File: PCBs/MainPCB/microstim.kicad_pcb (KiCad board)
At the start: 2 copper layers, 124.5 x 79.5 mm, 87 parts, among them J1 Conn_Coaxial, J10 Conn_Coaxial, J11 Screw_Terminal_01x02, J12 Conn_Coaxial, J3 Screw_Terminal_01x02, J5 Conn_Coaxial, J7 Screw_Terminal_01x02, J9 Screw_Terminal_01x02, U1 Teensy3.5, U10 AD7321, U11 INA826, U12 AD8276, U13 AD8276, U14 INA826, U15 OPA197, U16 DG509ACWE, U17 OPA197, U18 DG509ACWE, U19 DG419LDY, U2 CC3-0512DF-E, U20 DG419LDY, U3 L78L05_SO8, U4 L78L12_SO8, U5 ISO7760, U6 AD1582, U7 ISO7341C, U8 L79L12_SO8, U9 MCP4922

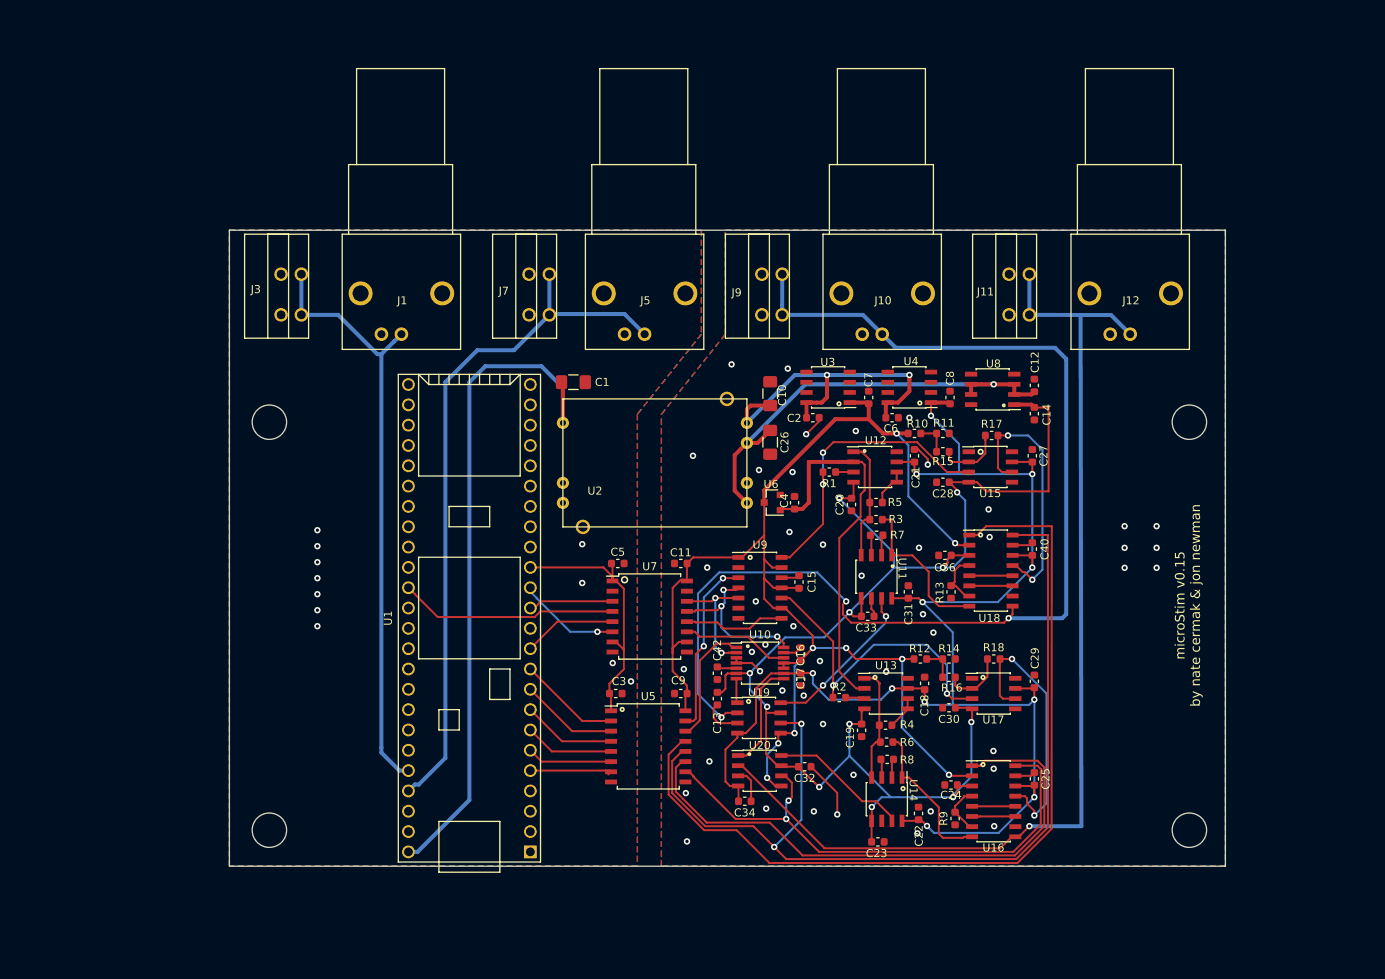
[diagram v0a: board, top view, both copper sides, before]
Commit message: almost done with revision 3. 12v regs removed, GPIO breakout and indicator LEDs added, layout cleaned up
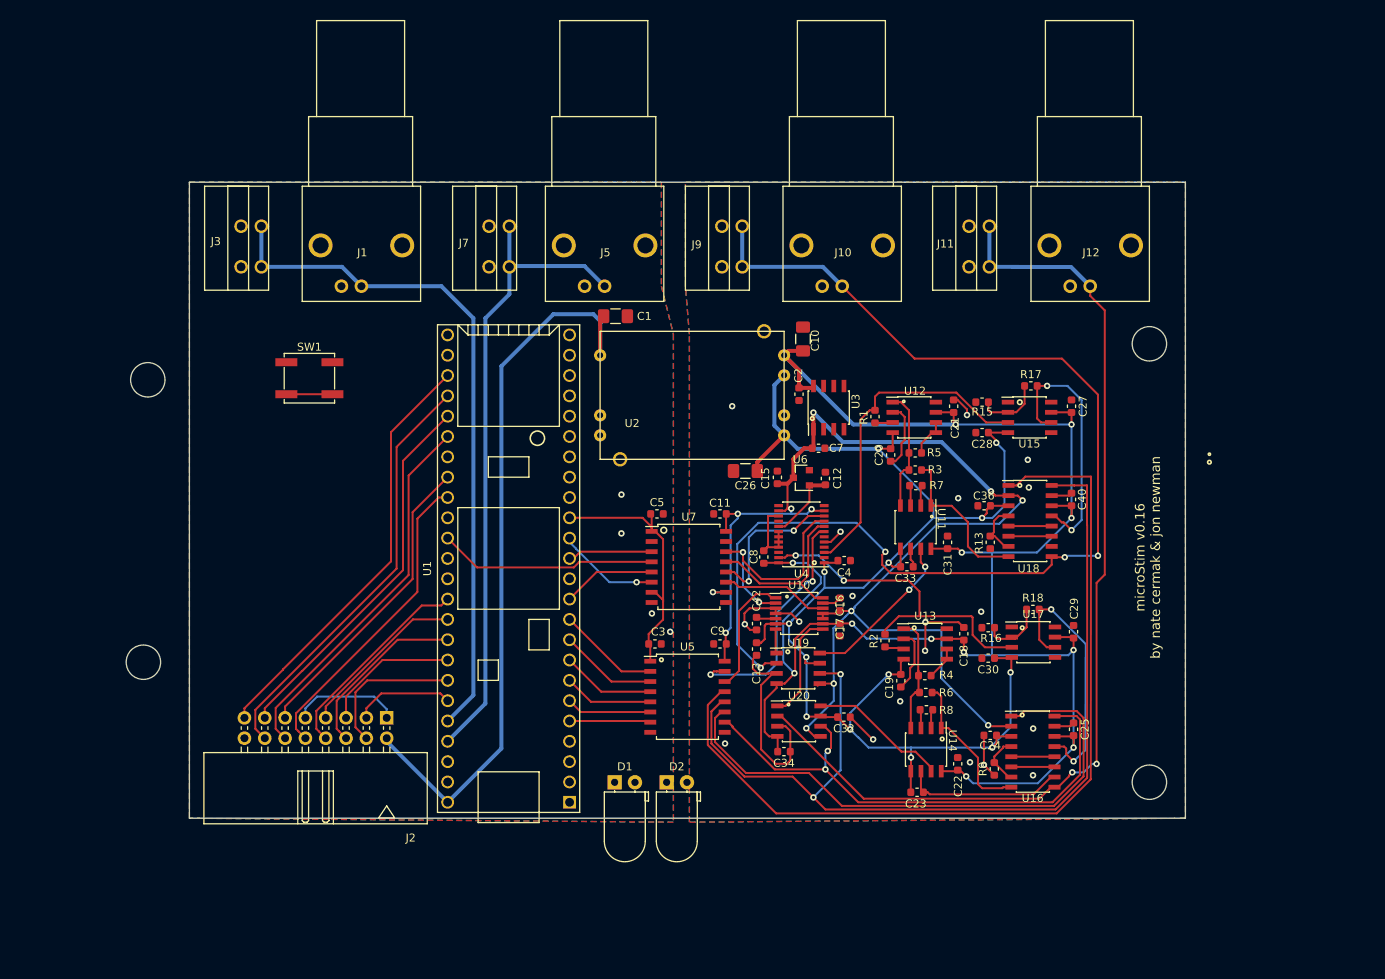
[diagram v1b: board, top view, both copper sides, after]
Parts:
- removed C14, C6: 1uF, Capacitor_SMD:C_0603_1608Metric
- removed R10, R12: 100, Resistor_SMD:R_0603_1608Metric
- removed R11, R14: 180, Resistor_SMD:R_0603_1608Metric
- removed U8: L79L12_SO8, Package_SO:SOIC-8_3.9x4.9mm_P1.27mm
- removed U9: MCP4922, Package_SO:SOIC-14_3.9x8.7mm_P1.27mm
- added D1: LED, LED_THT:LED_D5.0mm_Horizontal_O1.27mm_Z3.0mm, F.Cu at (135.7, 127.0)
- added D2: LED, LED_THT:LED_D5.0mm_Horizontal_O1.27mm_Z3.0mm, F.Cu at (142.2, 127.0)
- added J2: Conn_02x08_Counter_Clockwise, Connector_Multicomp:Multicomp_MC9A22-1634_2x08_P2.54mm_Horizontal, F.Cu at (107.2, 119.0)
- added SW1: SW_Push, Button_Switch_SMD:SW_SPST_EVPBF, F.Cu at (97.5, 76.5)
- C4, C8: value 1uF -> 0.1uF
- R17, R18: value 4k -> 500
- R3, R6: value 250 -> 100
- R7, R8: value 1.2k -> 1.8k
- U4: value L78L12_SO8 -> AD5752; footprint Package_SO:SOIC-8_3.9x4.9mm_P1.27mm -> Package_SO:TSSOP-24_4.4x7.8mm_P0.65mm
- moved C8 30.6 mm to (154.3, 98.8)
- moved C12 28.6 mm to (162.0, 89.0)
- moved H1 26.2 mm to (76.8, 112.0)
- moved U4 22.8 mm to (159.0, 96.0)
- moved H3 16.1 mm to (77.3, 76.7)
- moved C15 13.4 mm to (156.0, 88.9)
- moved H2 11.0 mm to (202.5, 72.2)
- moved C1 9.79 mm to (135.8, 68.8)
- moved U2 9.64 mm to (133.8, 86.6)
- moved C4 9.53 mm to (164.3, 99.3), turned to 180 degrees
- moved R2 9.14 mm to (169.4, 109.3), turned to 90 degrees
- moved R1 8.98 mm to (168.2, 81.3), turned to 90 degrees
- moved C7 8.92 mm to (161.1, 85.3), turned to 180 degrees
- moved U17 8.11 mm to (188.0, 109.5)
- moved C10 7.97 mm to (159.2, 71.6)
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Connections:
- C12 pad 2: -15V -> 2.5V
- C13 pad 1: -12V -> -15V
- C16 pad 1: +12V -> +15V
- C18 pad 2: +12V -> +15V
- C19 pad 1: -12V -> -15V
- C20 pad 1: -12V -> -15V
- C21 pad 2: +12V -> +15V
- C22 pad 2: +12V -> +15V
- C23 pad 2: -12V -> -15V
- C24 pad 2: -12V -> -15V
- C25 pad 2: +12V -> +15V
- C27 pad 2: +12V -> +15V
- C28 pad 1: -12V -> -15V
- C29 pad 2: +12V -> +15V
- C30 pad 1: -12V -> -15V
- C31 pad 2: +12V -> +15V
- C32 pad 2: -12V -> -15V
- C33 pad 2: -12V -> -15V
- C34 pad 2: +12V -> +15V
- C36 pad 2: -12V -> -15V
- C4 pad 2: 2.5V -> -15V
- C40 pad 2: +12V -> +15V
- C8 pad 2: +12V -> +15V
- R15 pad 1: Net-(R10-Pad1) -> GNDREF
- R16 pad 1: Net-(R12-Pad1) -> GNDREF
- U1 pad 39: Net-(U1-Pad39) -> GND
- U1 pad 43: Net-(U1-Pad43) -> GPIO5
- U1 pad 44: Net-(U1-Pad44) -> GPIO4
- U1 pad 45: Net-(U1-Pad45) -> GPIO3
- U1 pad 46: Net-(U1-Pad46) -> GPIO2
- U1 pad 47: Net-(U1-Pad47) -> GPIO1
- U1 pad 48: Net-(U1-Pad48) -> GPIO0
- U1 pad 51: +3V3 -> Net-(U1-Pad51)
- U10 pad 6: -12V -> -15V
- U10 pad 9: +12V -> +15V
- U11 pad 5: -12V -> -15V
- U11 pad 8: +12V -> +15V
- U12 pad 2: 2.5V -> GNDREF
- U12 pad 4: -12V -> -15V
- U12 pad 7: +12V -> +15V
- U13 pad 2: 2.5V -> GNDREF
- U13 pad 4: -12V -> -15V
- U13 pad 7: +12V -> +15V
- U14 pad 5: -12V -> -15V
- U14 pad 8: +12V -> +15V
- U15 pad 4: -12V -> -15V
- U15 pad 7: +12V -> +15V
- U16 pad 14: +12V -> +15V
- U16 pad 3: -12V -> -15V
- U17 pad 4: -12V -> -15V
- U17 pad 7: +12V -> +15V
- U18 pad 14: +12V -> +15V
- U18 pad 3: -12V -> -15V
- U19 pad 4: +12V -> +15V
- U19 pad 7: -12V -> -15V
- U20 pad 4: +12V -> +15V
- U20 pad 7: -12V -> -15V
- U4 pad 1: +12V -> -15V
- U4 pad 2: GNDREF -> (no net)
- U4 pad 3: GNDREF -> DAC0
- U4 pad 4: Net-(U4-Pad4) -> (no net)
- U4 pad 5: Net-(U4-Pad5) -> GNDREF
- U4 pad 6: GNDREF -> (no net)
- U4 pad 7: GNDREF -> CS0i
- U4 pad 8: +15V -> SCK0i
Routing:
- net +12V: track 182.1 -> 0.00 mm, vias 11 -> 0
- net +15V: track 42.4 -> 223.0 mm, vias 2 -> 12
- net -12V: track 174.8 -> 0.00 mm, vias 11 -> 0
- net -15V: track 56.8 -> 183.3 mm, vias 1 -> 13
- net GNDREF: track 38.7 -> 117.1 mm, vias 46 -> 19
- net Net-(J2-Pad15): track 0.00 -> 53.3 mm
- net Net-(J2-Pad14): track 0.00 -> 53.2 mm
- net Net-(J2-Pad13): track 0.00 -> 47.2 mm
- net Net-(J2-Pad12): track 0.00 -> 47.1 mm
- net Net-(J2-Pad10): track 0.00 -> 39.1 mm
- net Net-(J2-Pad11): track 0.00 -> 38.5 mm
- net 2.5V: track 47.4 -> 9.22 mm
- net GPIO5: track 0.00 -> 26.1 mm
- net GPIO3: track 0.00 -> 22.2 mm
- net GPIO4: track 0.00 -> 21.2 mm
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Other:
- board text added: "microStim v0.16 by nate cermak & jon newman"
- board text removed: "microStim v0.15 by nate cermak & jon newman"

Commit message: major updates to isolate each output channel.
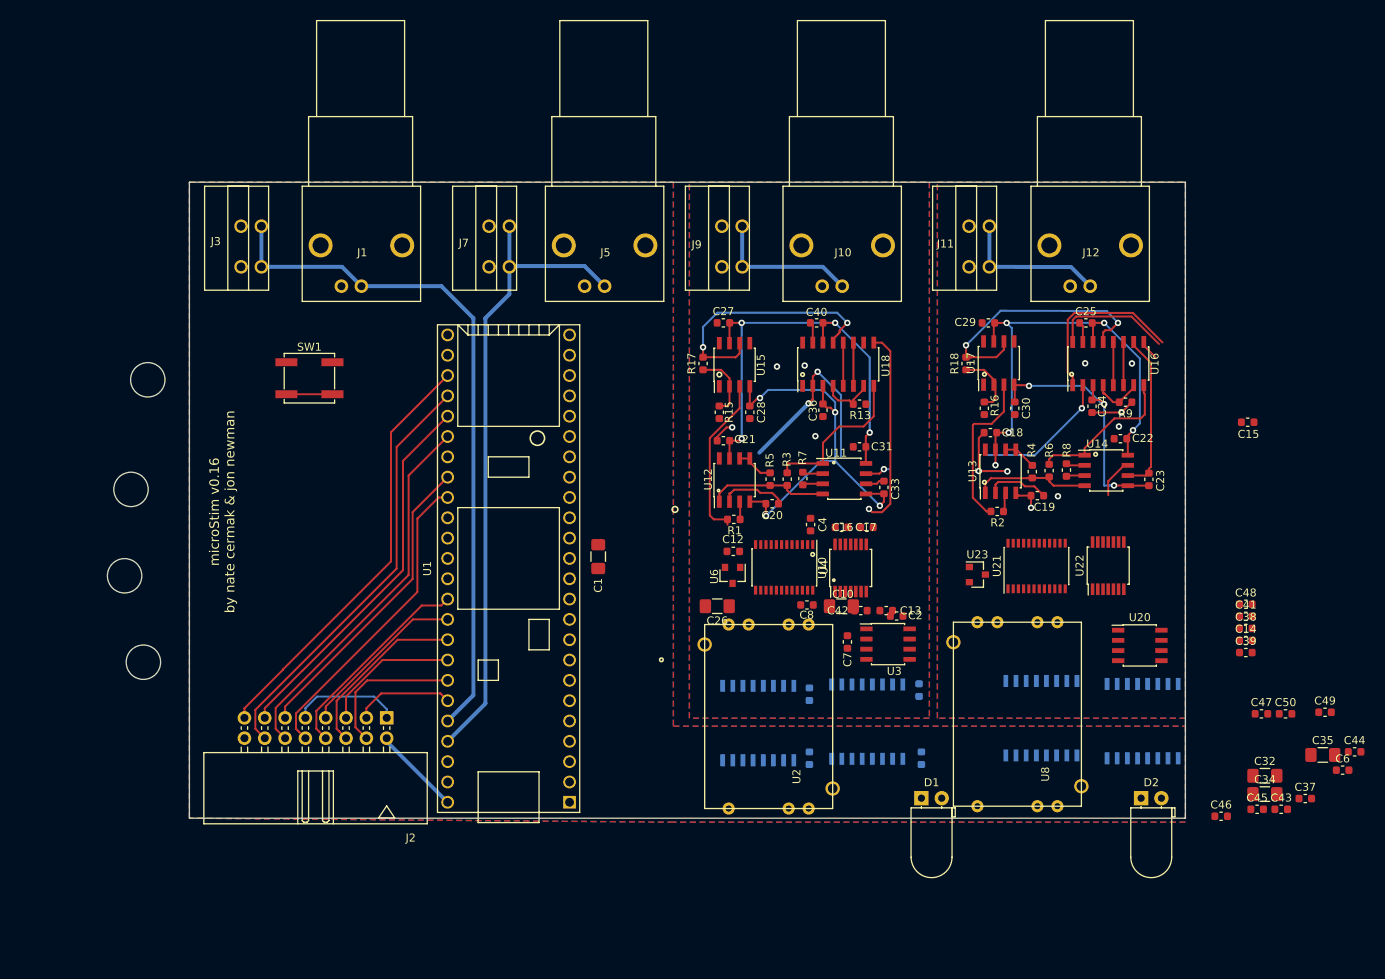
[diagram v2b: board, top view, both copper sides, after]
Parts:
- added C14: 0.1uF, Capacitor_SMD:C_0603_1608Metric, F.Cu at (214.6, 109.3)
- added C35: 10uF, Capacitor_SMD:C_1206_3216Metric_Pad1.42x1.75mm_HandSolder, F.Cu at (224.2, 123.6)
- added C37: 0.1uF, Capacitor_SMD:C_0603_1608Metric, F.Cu at (222.0, 129.0)
- added C38: 0.1uF, Capacitor_SMD:C_0603_1608Metric, F.Cu at (214.6, 107.8)
- added C39: 1uF, Capacitor_SMD:C_0603_1608Metric, F.Cu at (214.6, 110.8)
- added C41: 0.1uF, Capacitor_SMD:C_0603_1608Metric, F.Cu at (214.6, 106.3)
- added C43: 680nF, Capacitor_SMD:C_0603_1608Metric, F.Cu at (219.0, 130.4)
- added C44: 0.1uF, Capacitor_SMD:C_0603_1608Metric, F.Cu at (228.2, 123.2)
- added C45: 1uF, Capacitor_SMD:C_0603_1608Metric, F.Cu at (216.0, 130.4)
- added C46: 0.1uF, Capacitor_SMD:C_0603_1608Metric, F.Cu at (211.5, 131.3)
- added C47: 0.1uF, Capacitor_SMD:C_0603_1608Metric, F.Cu at (216.5, 118.5)
- added C48: 1uF, Capacitor_SMD:C_0603_1608Metric, F.Cu at (214.6, 104.8)
- added C49: 0.1uF, Capacitor_SMD:C_0603_1608Metric, F.Cu at (224.5, 118.3)
- added C50: 0.1uF, Capacitor_SMD:C_0603_1608Metric, F.Cu at (219.5, 118.5)
- added C6: 0.1uF, Capacitor_SMD:C_0603_1608Metric, F.Cu at (226.7, 125.5)
- added U21: AD5752, Package_SO:TSSOP-24_4.4x7.8mm_P0.65mm, F.Cu at (188.4, 100.0)
- added U22: AD7321, Package_SO:TSSOP-14_4.4x5mm_P0.65mm, F.Cu at (197.4, 99.9)
- added U23: AD1582, Package_TO_SOT_SMD:SOT-23, F.Cu at (181.0, 101.0)
- added U8: CC3-0512DF-E, microstim:CC3-0512DF-E, F.Cu at (194.0, 130.0)
- added U9: ISO7760, Package_SO:SOIC-16W_7.5x10.3mm_P1.27mm, B.Cu at (189.0, 119.0)
- C11, C3, C5, C9, U5, U7: moved to B.Cu
- C32, C34: value 0.1uF -> 10uF; footprint Capacitor_SMD:C_0603_1608Metric -> Capacitor_SMD:C_1206_3216Metric_Pad1.42x1.75mm_HandSolder
- U19: value DG419LDY -> ISO7341C; footprint Package_SO:SOIC-8_3.9x4.9mm_P1.27mm -> Package_SO:SOIC-16W_7.5x10.3mm_P1.27mm; moved to B.Cu
- U20: value DG419LDY -> L78L05_SO8
- moved H4 130.7 mm to (74.4, 101.2)
- moved H2 128.6 mm to (75.2, 90.4)
- moved C34 60.3 mm to (216.9, 128.5), turned to 0 degrees
- moved D2 59.3 mm to (201.5, 129.0)
- moved C15 59.2 mm to (214.8, 82.0), turned to 0 degrees
- moved C32 53.1 mm to (216.9, 126.2), turned to 0 degrees
- moved U2 52.4 mm to (162.9, 130.3), turned to 90 degrees
- moved C25 50.8 mm to (194.6, 69.6), turned to 0 degrees
- moved U16 49.4 mm to (197.4, 74.7), turned to 90 degrees
- moved R9 48.7 mm to (199.5, 79.5), turned to 180 degrees
- moved C23 48.7 mm to (202.4, 89.1), turned to 270 degrees
- moved C22 45.4 mm to (198.9, 84.1), turned to 0 degrees
- moved C5 45.0 mm to (174.0, 124.0), turned to 90 degrees
- moved C27 44.7 mm to (149.2, 69.6), turned to 0 degrees
- moved U20 43.6 mm to (201.3, 109.9)
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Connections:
- net 2.5V renamed 2.5V_0
- net CS0i renamed CS0_0i
- net CS1i renamed CS1_0i
- net DAC0 renamed DAC_0
- net IOUT0 renamed IOUT_0
- net IOUT1 renamed IOUT_1
- net MISO renamed MISO_0
- net MISOi renamed MISO_0i
- net MOSI renamed MOSI_0
- net MOSIi renamed MOSI_0i
- net NLDACi renamed NLDAC_0i
- net OE0i renamed OE0_0i
- net SCK0 renamed SCK_0
- net SCK0i renamed SCK_0i
- net VOUT0 renamed VOUT_0
- net VOUT1 renamed VOUT_1
- C10 pad 1: GNDREF -> GND_0
- C10 pad 2: +15V -> +15V_0
- C11 pad 1: +5V -> +5V_0
- C11 pad 2: GNDREF -> GND_0
- C12 pad 1: GNDREF -> GND_0
- C13 pad 1: -15V -> -15V_0
- C13 pad 2: GNDREF -> GND_0
- C15 pad 1: GNDREF -> GND_0
- C15 pad 2: +5V -> +5V_0
- C16 pad 1: +15V -> +15V_0
- C16 pad 2: GNDREF -> GND_0
- C17 pad 1: +5V -> +5V_0
- C17 pad 2: GNDREF -> GND_0
- C2 pad 1: GNDREF -> GND_0
- C2 pad 2: +15V -> +15V_0
- C20 pad 2: GNDREF -> GND_0
- C21 pad 1: GNDREF -> GND_0
- C26 pad 1: -15V -> -15V_0
- C26 pad 2: GNDREF -> GND_0
- C32 pad 1: GNDREF -> GND
- C32 pad 2: -15V -> VUSB
- C34 pad 1: GNDREF -> GND_1
- C34 pad 2: +15V -> +15V_1
- C4 pad 1: GNDREF -> GND_0
- C4 pad 2: -15V -> -15V_0
- C42 pad 2: GNDREF -> GND_0
- C7 pad 1: GNDREF -> GND_0
- C7 pad 2: +5V -> +5V_0
- C8 pad 1: GNDREF -> GND_0
- C8 pad 2: +15V -> +15V_0
- C9 pad 1: GNDREF -> GND_0
- C9 pad 2: +5V -> +5V_0
- J10 pad 1: OUT0 -> OUT_0
- J11 pad 1: OUT1 -> OUT_1
- J12 pad 1: OUT1 -> OUT_1
- J9 pad 1: OUT0 -> OUT_0
- R15 pad 1: GNDREF -> GND_0
- R2 pad 2: DAC1 -> DAC_1
- U1 pad 10: CS0 -> OE0_0
- U1 pad 11: NLDAC -> CS1_0
- U1 pad 12: Net-(U1-Pad12) -> CS0_0
- U1 pad 16: Net-(U1-Pad16) -> NLDAC_0
- U1 pad 2: Net-(U1-Pad2) -> MOSI_1
- U1 pad 24: Net-(U1-Pad24) -> SCK_1
- U1 pad 3: Net-(U1-Pad3) -> MISO_1
- U1 pad 4: Net-(U1-Pad4) -> OE1_1
- U1 pad 5: OE3 -> OE0_1
- U1 pad 50: Net-(J5-Pad1) -> GND
- U1 pad 6: OE2 -> CS1_1
- U1 pad 7: OE1 -> CS0_1
- U1 pad 8: OE0 -> NLDAC_1
- U1 pad 9: CS1 -> OE1_0
- U10 pad 10: +5V -> +5V_0
- U10 pad 11: +5V -> +5V_0
- U10 pad 13: GNDREF -> GND_0
- U10 pad 3: GNDREF -> GND_0
- U10 pad 4: GNDREF -> GND_0
- U10 pad 6: -15V -> -15V_0
- U10 pad 7: Net-(U10-Pad7) -> OUT_0
- U10 pad 8: Net-(U10-Pad8) -> ISENSE_0
- U10 pad 9: +15V -> +15V_0
- U11 pad 7: ISENSE0 -> ISENSE_0
- U12 pad 2: GNDREF -> GND_0
- U14 pad 7: ISENSE1 -> ISENSE_1
- U16 pad 1: OE2i -> OE0_1i
- U16 pad 16: OE3i -> OE1_1i
- U16 pad 9: OUT1 -> OUT_1
- U17 pad 3: DAC1 -> DAC_1
- U18 pad 16: OE1i -> OE1_0i
- U18 pad 9: OUT0 -> OUT_0
- U19 pad 1: Net-(U10-Pad7) -> +3V3
- U19 pad 2: OUT0 -> GND
- U19 pad 3: GNDREF -> MOSI_1
- U19 pad 4: +15V -> SCK_1
- U19 pad 5: +5V -> NLDAC_1
- U19 pad 6: OE1i -> MISO_1
- U19 pad 7: -15V -> +3V3
- U19 pad 8: ISENSE0 -> GND
- U2 pad 4: -15V -> -15V_0
- U2 pad 5: GNDREF -> GND_0
- U2 pad 6: -15V -> -15V_0
- U2 pad 7: +15V -> +15V_0
- U20 pad 1: Net-(U10-Pad8) -> +5V_1
- U20 pad 2: OUT1 -> GND_1
- U20 pad 3: GNDREF -> GND_1
- U20 pad 4: +15V -> Net-(U20-Pad4)
- U20 pad 5: +5V -> Net-(U20-Pad5)
- U20 pad 6: OE3i -> GND_1
- U20 pad 7: -15V -> GND_1
- U20 pad 8: ISENSE1 -> +15V_1
- U3 pad 1: +5V -> +5V_0
- U3 pad 2: GNDREF -> GND_0
- U3 pad 3: GNDREF -> GND_0
- U3 pad 6: GNDREF -> GND_0
- U3 pad 7: GNDREF -> GND_0
- U3 pad 8: +15V -> +15V_0
- U4 pad 1: -15V -> -15V_0
- U4 pad 11: +5V -> +5V_0
- U4 pad 14: +5V -> +5V_0
- U4 pad 15: GNDREF -> GND_0
- U4 pad 18: GNDREF -> GND_0
- U4 pad 19: GNDREF -> GND_0
- U4 pad 20: GNDREF -> GND_0
- U4 pad 21: GNDREF -> GND_0
- U4 pad 23: DAC1 -> Net-(U4-Pad23)
- U4 pad 24: +15V -> +15V_0
- U4 pad 5: GNDREF -> GND_0
- U5 pad 10: OE3i -> Net-(U5-Pad10)
- U5 pad 11: OE2i -> Net-(U5-Pad11)
- U5 pad 12: OE1i -> OE1_0i
- U5 pad 16: +5V -> +5V_0
- U5 pad 2: CS0 -> CS0_0
- U5 pad 3: CS1 -> CS1_0
- U5 pad 4: OE0 -> OE0_0
- U5 pad 5: OE1 -> OE1_0
- U5 pad 6: OE2 -> Net-(U5-Pad6)
- U5 pad 7: OE3 -> Net-(U5-Pad7)
- U5 pad 9: GNDREF -> GND_0
- U6 pad 2: GNDREF -> GND_0
- U6 pad 3: +5V -> +5V_0
- U7 pad 10: +5V -> +5V_0
- U7 pad 15: GNDREF -> GND_0
- U7 pad 16: +5V -> +5V_0
- U7 pad 5: NLDAC -> NLDAC_0
- U7 pad 9: GNDREF -> GND_0
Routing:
- net OUT0: track 147.1 -> 0.00 mm, vias 4 -> 0
- net +5V: track 168.4 -> 42.2 mm, vias 12 -> 3
- net OUT1: track 125.6 -> 0.00 mm, vias 2 -> 0
- net OE1i: track 119.1 -> 0.00 mm, vias 2 -> 0
- net OE0_0i: track 109.6 -> 0.00 mm
- net +15V: track 223.0 -> 117.0 mm, vias 12 -> 9
- net -15V: track 183.3 -> 90.6 mm, vias 13 -> 8
- net VUSB: track 93.3 -> 11.2 mm
- net OE2i: track 72.4 -> 0.00 mm
- net GNDREF: track 117.1 -> 49.8 mm, vias 19 -> 10
- net OE3i: track 66.8 -> 0.00 mm, vias 2 -> 0
- net OUT_0: track 0.00 -> 43.4 mm, vias 0 -> 1
- net DAC1: track 42.7 -> 0.00 mm, vias 2 -> 0
- net +3V3: track 33.5 -> 0.00 mm
- net CS0_0i: track 30.4 -> 0.00 mm, vias 2 -> 0
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- added copper zone on B.Cu, net GND_0
- added copper zone on F.Cu, net GND_0
- added copper zone on B.Cu, net GND_1
- added copper zone on F.Cu, net GND_1
- removed copper zone on B.Cu, net GNDREF
- removed copper zone on F.Cu, net GNDREF
